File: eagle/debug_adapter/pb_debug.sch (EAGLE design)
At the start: 29 parts, among them J1 JTAG_14PIN_FULL, U1 MAX9910

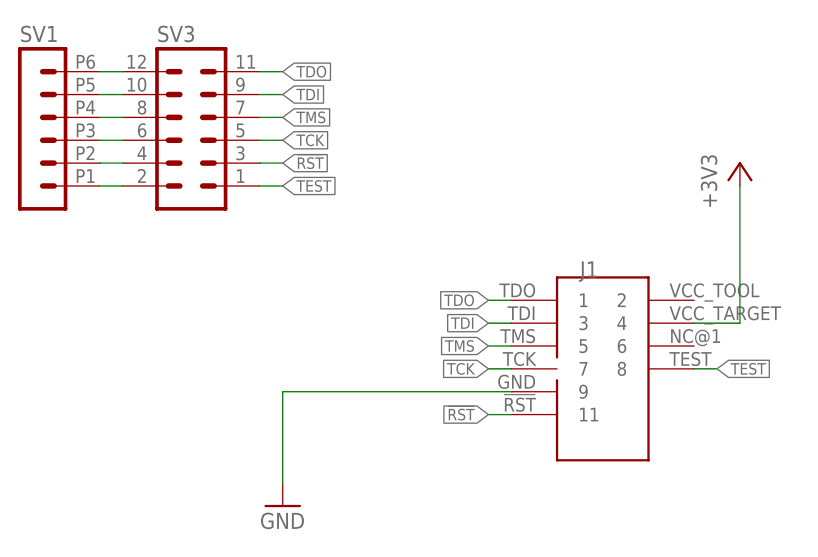
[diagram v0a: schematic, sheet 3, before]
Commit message: moved some pins in debug adapter
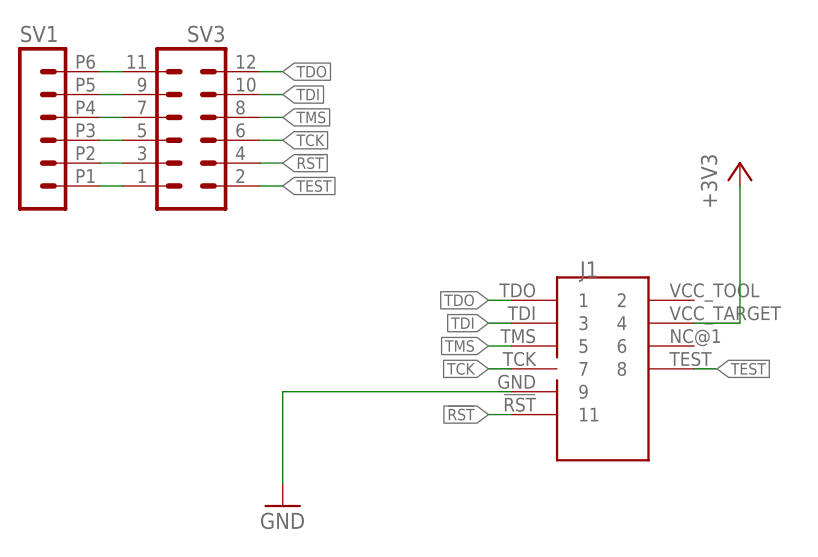
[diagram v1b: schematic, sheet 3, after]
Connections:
- net !RST!: now also SV3.4; no longer SV3.3
- net N$14: now also SV3.9; no longer SV3.10
- net N$15: now also SV3.7; no longer SV3.8
- net N$16: now also SV3.5; no longer SV3.6
- net N$17: now also SV3.3; no longer SV3.4
- net N$18: now also SV3.1; no longer SV3.2
- net N$7: now also SV3.11; no longer SV3.12
- net TCK: now also SV3.6; no longer SV3.5
- net TDI: now also SV3.10; no longer SV3.9
- net TDO: now also SV3.12; no longer SV3.11
- net TEST: now also SV3.2; no longer SV3.1
- net TMS: now also SV3.8; no longer SV3.7
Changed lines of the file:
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@@
 <instance part="GND1" gate="1" x="-35.56" y="-15.24"/>
 <instance part="SV1" gate="1" x="-63.5" y="27.94"/>
-<instance part="SV3" gate="1" x="-45.72" y="27.94"/>
+<instance part="SV3" gate="1" x="-45.72" y="27.94" rot="MR0"/>
 </instances>
 <busses>
@@
 </segment>
 <segment>
-<pinref part="SV3" gate="1" pin="11"/>
+<pinref part="SV3" gate="1" pin="12"/>
 <wire x1="-35.56" y1="33.02" x2="-38.1" y2="33.02" width="0.1524" layer="91"/>
 <label x="-35.56" y="33.02" size="1.27" layer="95" xref="yes"/>
@@
 </segment>
 <segment>
-<pinref part="SV3" gate="1" pin="9"/>
+<pinref part="SV3" gate="1" pin="10"/>
 <wire x1="-35.56" y1="30.48" x2="-38.1" y2="30.48" width="0.1524" layer="91"/>
 <label x="-35.56" y="30.48" size="1.27" layer="95" xref="yes"/>
@@
 </segment>
 <segment>
-<pinref part="SV3" gate="1" pin="7"/>
+<pinref part="SV3" gate="1" pin="8"/>
 <wire x1="-35.56" y1="27.94" x2="-38.1" y2="27.94" width="0.1524" layer="91"/>
 <label x="-35.56" y="27.94" size="1.27" layer="95" xref="yes"/>
@@
 </segment>
 <segment>
-<pinref part="SV3" gate="1" pin="5"/>
+<pinref part="SV3" gate="1" pin="6"/>
 <wire x1="-35.56" y1="25.4" x2="-38.1" y2="25.4" width="0.1524" layer="91"/>
 <label x="-35.56" y="25.4" size="1.27" layer="95" xref="yes"/>
@@
 </segment>
 <segment>
-<pinref part="SV3" gate="1" pin="3"/>
+<pinref part="SV3" gate="1" pin="4"/>
 <wire x1="-35.56" y1="22.86" x2="-38.1" y2="22.86" width="0.1524" layer="91"/>
 <label x="-35.56" y="22.86" size="1.27" layer="95" xref="yes"/>
@@
 </segment>
 <segment>
-<pinref part="SV3" gate="1" pin="1"/>
+<pinref part="SV3" gate="1" pin="2"/>
 <wire x1="-35.56" y1="20.32" x2="-38.1" y2="20.32" width="0.1524" layer="91"/>
 <label x="-35.56" y="20.32" size="1.27" layer="95" xref="yes"/>
@@
 <net name="N$7" class="0">
 <segment>
-<pinref part="SV3" gate="1" pin="12"/>
 <pinref part="SV1" gate="1" pin="6"/>
-<wire x1="-53.34" y1="33.02" x2="-55.88" y2="33.02" width="0.1524" layer="91"/>
+<pinref part="SV3" gate="1" pin="11"/>
+<wire x1="-55.88" y1="33.02" x2="-53.34" y2="33.02" width="0.1524" layer="91"/>
 </segment>
 </net>
 <net name="N$14" class="0">
 <segment>
-<pinref part="SV3" gate="1" pin="10"/>
 <pinref part="SV1" gate="1" pin="5"/>
-<wire x1="-53.34" y1="30.48" x2="-55.88" y2="30.48" width="0.1524" layer="91"/>
+<pinref part="SV3" gate="1" pin="9"/>
+<wire x1="-55.88" y1="30.48" x2="-53.34" y2="30.48" width="0.1524" layer="91"/>
 </segment>
 </net>
 <net name="N$15" class="0">
 <segment>
-<pinref part="SV3" gate="1" pin="8"/>
 <pinref part="SV1" gate="1" pin="4"/>
-<wire x1="-53.34" y1="27.94" x2="-55.88" y2="27.94" width="0.1524" layer="91"/>
+<pinref part="SV3" gate="1" pin="7"/>
+<wire x1="-55.88" y1="27.94" x2="-53.34" y2="27.94" width="0.1524" layer="91"/>
 </segment>
 </net>
 <net name="N$16" class="0">
 <segment>
-<pinref part="SV3" gate="1" pin="6"/>
 <pinref part="SV1" gate="1" pin="3"/>
-<wire x1="-53.34" y1="25.4" x2="-55.88" y2="25.4" width="0.1524" layer="91"/>
+<pinref part="SV3" gate="1" pin="5"/>
+<wire x1="-55.88" y1="25.4" x2="-53.34" y2="25.4" width="0.1524" layer="91"/>
 </segment>
 </net>
 <net name="N$17" class="0">
 <segment>
-<pinref part="SV3" gate="1" pin="4"/>
 <pinref part="SV1" gate="1" pin="2"/>
-<wire x1="-53.34" y1="22.86" x2="-55.88" y2="22.86" width="0.1524" layer="91"/>
+<pinref part="SV3" gate="1" pin="3"/>
+<wire x1="-55.88" y1="22.86" x2="-53.34" y2="22.86" width="0.1524" layer="91"/>
 </segment>
 </net>
 <net name="N$18" class="0">
 <segment>
-<pinref part="SV3" gate="1" pin="2"/>
 <pinref part="SV1" gate="1" pin="1"/>
-<wire x1="-53.34" y1="20.32" x2="-55.88" y2="20.32" width="0.1524" layer="91"/>
+<pinref part="SV3" gate="1" pin="1"/>
+<wire x1="-55.88" y1="20.32" x2="-53.34" y2="20.32" width="0.1524" layer="91"/>
 </segment>
 </net>

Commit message: finished pb debug board
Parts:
- added J2: MA02-1STR, con-lstb:MA02-1STR
- added LED1: (no value), SparkFun-LED:LED0603
- added Q1: 2N7002, nav:2N7002
- added R8: (no value), rcl:R-US_R0603
- added R9: 240, rcl:R-US_R0603
- added TP17: TP_STD, skyspecs:TP_STD
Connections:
- new net LED: Q1.G, R8.2, TP17.P$1
- new net N$22: LED1.C, Q1.D
- new net N$23: LED1.A, R9.1
- new net N$24: J2.2, R9.2
- net +3V3: now also J2.1
- net GND: now also Q1.S
- net N$10: now also R8.1
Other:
- note added: "Optional LED"
- moved on the sheet: TP10, TP11, TP12
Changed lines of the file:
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@@
 <part name="GND5" library="supply1" deviceset="GND" device=""/>
 <part name="+3V4" library="supply1" deviceset="+3V3" device=""/>
+<part name="R8" library="rcl" deviceset="R-US_" device="R0603"/>
+<part name="TP17" library="skyspecs" deviceset="TP" device="_STD"/>
+<part name="Q1" library="nav" deviceset="2N7002" device=""/>
+<part name="R9" library="rcl" deviceset="R-US_" device="R0603" value="240"/>
+<part name="LED1" library="SparkFun-LED" deviceset="LED" device="0603"/>
+<part name="J2" library="con-lstb" deviceset="MA02-1" device="STR"/>
+<part name="+3V5" library="supply1" deviceset="+3V3" device=""/>
+<part name="GND6" library="supply1" deviceset="GND" device=""/>
 </parts>
 <sheets>
@@
 <description>12-pin 1.27mm Connector</description>
 <plain>
+<text x="96.52" y="33.02" size="1.778" layer="95">Optional LED</text>
 </plain>
 <instances>
@@
 <instance part="TP8" gate="G$1" x="38.1" y="-17.78"/>
 <instance part="TP9" gate="G$1" x="38.1" y="-25.4"/>
-<instance part="TP10" gate="G$1" x="38.1" y="-33.02"/>
-<instance part="TP11" gate="G$1" x="38.1" y="-40.64"/>
-<instance part="TP12" gate="G$1" x="38.1" y="-48.26"/>
+<instance part="TP10" gate="G$1" x="38.1" y="-38.1"/>
+<instance part="TP11" gate="G$1" x="38.1" y="-45.72"/>
+<instance part="TP12" gate="G$1" x="38.1" y="-53.34"/>
 <instance part="R1" gate="G$1" x="50.8" y="45.72"/>
 <instance part="R2" gate="G$1" x="50.8" y="10.16"/>
@@
 <instance part="TP14" gate="G$1" x="68.58" y="10.16"/>
 <instance part="TP15" gate="G$1" x="68.58" y="-2.54"/>
+<instance part="R8" gate="G$1" x="50.8" y="-30.48"/>
+<instance part="TP17" gate="G$1" x="81.28" y="-30.48"/>
+<instance part="Q1" gate="G$1" x="101.6" y="-17.78"/>
+<instance part="R9" gate="G$1" x="101.6" y="5.08" rot="R90"/>
+<instance part="LED1" gate="G$1" x="101.6" y="-5.08"/>
+<instance part="J2" gate="G$1" x="109.22" y="17.78" rot="MR0"/>
+<instance part="+3V5" gate="G$1" x="101.6" y="27.94"/>
+<instance part="GND6" gate="1" x="101.6" y="-30.48"/>
 </instances>
 <busses>
@@
 <wire x1="22.86" y1="-25.4" x2="33.02" y2="-25.4" width="0.1524" layer="91"/>
 <pinref part="TP9" gate="G$1" pin="P$1"/>
+<wire x1="22.86" y1="-25.4" x2="22.86" y2="-30.48" width="0.1524" layer="91"/>
+<junction x="22.86" y="-25.4"/>
+<pinref part="R8" gate="G$1" pin="1"/>
+<wire x1="22.86" y1="-30.48" x2="45.72" y2="-30.48" width="0.1524" layer="91"/>
 </segment>
 </net>
@@
 <pinref part="SV2" gate="1" pin="3"/>
 <wire x1="7.62" y1="-7.62" x2="20.32" y2="-7.62" width="0.1524" layer="91"/>
-<wire x1="20.32" y1="-7.62" x2="20.32" y2="-33.02" width="0.1524" layer="91"/>
+<wire x1="20.32" y1="-7.62" x2="20.32" y2="-38.1" width="0.1524" layer="91"/>
 <pinref part="TP10" gate="G$1" pin="P$1"/>
-<wire x1="20.32" y1="-33.02" x2="33.02" y2="-33.02" width="0.1524" layer="91"/>
+<wire x1="20.32" y1="-38.1" x2="33.02" y2="-38.1" width="0.1524" layer="91"/>
 </segment>
 </net>
@@
 <pinref part="SV2" gate="1" pin="2"/>
 <wire x1="7.62" y1="-10.16" x2="17.78" y2="-10.16" width="0.1524" layer="91"/>
-<wire x1="17.78" y1="-10.16" x2="17.78" y2="-40.64" width="0.1524" layer="91"/>
+<wire x1="17.78" y1="-10.16" x2="17.78" y2="-45.72" width="0.1524" layer="91"/>
 <pinref part="TP11" gate="G$1" pin="P$1"/>
-<wire x1="17.78" y1="-40.64" x2="33.02" y2="-40.64" width="0.1524" layer="91"/>
+<wire x1="17.78" y1="-45.72" x2="33.02" y2="-45.72" width="0.1524" layer="91"/>
 </segment>
 </net>
@@
 <pinref part="SV2" gate="1" pin="1"/>
 <wire x1="7.62" y1="-12.7" x2="15.24" y2="-12.7" width="0.1524" layer="91"/>
-<wire x1="15.24" y1="-12.7" x2="15.24" y2="-48.26" width="0.1524" layer="91"/>
+<wire x1="15.24" y1="-12.7" x2="15.24" y2="-53.34" width="0.1524" layer="91"/>
 <pinref part="TP12" gate="G$1" pin="P$1"/>
-<wire x1="15.24" y1="-48.26" x2="33.02" y2="-48.26" width="0.1524" layer="91"/>
+<wire x1="15.24" y1="-53.34" x2="33.02" y2="-53.34" width="0.1524" layer="91"/>
 </segment>
 </net>
@@
 <junction x="58.42" y="10.16"/>
 </segment>
+<segment>
+<pinref part="J2" gate="G$1" pin="1"/>
+<pinref part="+3V5" gate="G$1" pin="+3V3"/>
+<wire x1="104.14" y1="20.32" x2="101.6" y2="20.32" width="0.1524" layer="91"/>
+<wire x1="101.6" y1="20.32" x2="101.6" y2="25.4" width="0.1524" layer="91"/>
+</segment>
 </net>
 <net name="GND" class="0">
@@
 <junction x="58.42" y="-2.54"/>
 </segment>
-</net>
+<segment>
+<pinref part="Q1" gate="G$1" pin="S"/>
+<pinref part="GND6" gate="1" pin="GND"/>
+<wire x1="101.6" y1="-22.86" x2="101.6" y2="-27.94" width="0.1524" layer="91"/>
+</segment>
+</net>
+<net name="LED" class="0">
+<segment>
+<pinref part="R8" gate="G$1" pin="2"/>
+<pinref part="TP17" gate="G$1" pin="P$1"/>
+<wire x1="55.88" y1="-30.48" x2="68.58" y2="-30.48" width="0.1524" layer="91"/>
+<label x="56.896" y="-30.48" size="1.524" layer="95"/>
+<pinref part="Q1" gate="G$1" pin="G"/>
+<wire x1="68.58" y1="-30.48" x2="76.2" y2="-30.48" width="0.1524" layer="91"/>
+<wire x1="96.52" y1="-17.78" x2="68.58" y2="-17.78" width="0.1524" layer="91"/>
+<wire x1="68.58" y1="-17.78" x2="68.58" y2="-30.48" width="0.1524" layer="91"/>
+<junction x="68.58" y="-30.48"/>
+</segment>
+</net>
+<net name="N$22" class="0">
+<segment>
+<pinref part="LED1" gate="G$1" pin="C"/>
+<pinref part="Q1" gate="G$1" pin="D"/>
+<wire x1="101.6" y1="-10.16" x2="101.6" y2="-12.7" width="0.1524" layer="91"/>
+</segment>
+</net>
+<net name="N$23" class="0">
+<segment>
+<pinref part="LED1" gate="G$1" pin="A"/>
+<pinref part="R9" gate="G$1" pin="1"/>
+<wire x1="101.6" y1="-2.54" x2="101.6" y2="0" width="0.1524" layer="91"/>
+</segment>
+</net>
+<net name="N$24" class="0">
+<segment>
+<pinref part="R9" gate="G$1" pin="2"/>
+<wire x1="101.6" y1="10.16" x2="101.6" y2="17.78" width="0.1524" layer="91"/>
+<pinref part="J2" gate="G$1" pin="2"/>
+<wire x1="101.6" y1="17.78" x2="104.14" y2="17.78" width="0.1524" layer="91"/>
+</segment>
+</net>
